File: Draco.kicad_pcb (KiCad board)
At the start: 2 copper layers, 114.3 x 44.5 mm, 117 parts, among them J1 Conn_01x03, J10 Conn_01x03, J11 Conn_01x06, J12 Conn_02x05_Odd_Even, J13 Conn_01x04, J14 Conn_01x01, J15 Micro_SD_Card, J16 Conn_01x03, J17 CHARGE_A, J18 CHARGE_C, J19 CHARGE_B, J2 Conn_01x03, J20 Conn_01x04, J3 Conn_01x03, J4 Conn_01x03, J5 Conn_01x03, J6 Conn_01x03, J7 Conn_01x03, J8 Conn_01x03, J9 Conn_01x03, Q1 BC817, Q2 Q_NMOS_DGS, Q3 BC817, Q4 Q_NMOS_DGS, Q5 BC817, Q6 Q_NMOS_DGS, U1 ATMEGA2560-16AU, U2 LOGIC-TXS0108EPWR(TSSOP20), U3 RFM95HW, U4 TPS54332, U5 TLV62568, U6 SAM-M8Q, U7 BMX055, U8 MS5607, Y1 16MHz

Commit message: Routed 60%
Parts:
- removed J14: Conn_01x01, Pin_Headers:Pin_Header_Straight_1x01_Pitch2.54mm
- BT1, C25, C26, R2, R3, U2, U6: moved to F.Cu
- moved U7 257.4 mm to (140.5, 82.6), turned to 90 degrees
- moved AE1 190.1 mm to (166.4, 112.1), turned to 90 degrees
- moved U2 188.1 mm to (156.5, 98.5), turned to 90 degrees
- moved C14 185.9 mm to (166.4, 106.9), turned to 270 degrees
- moved U3 170.0 mm to (178.0, 105.1), turned to 180 degrees
- moved C28 168.9 mm to (224.3, 119.8), turned to 90 degrees
- moved R6 167.9 mm to (231.4, 118.8)
- moved C27 165.6 mm to (226.3, 119.8), turned to 90 degrees
- moved R27 164.4 mm to (236.0, 127.5)
- moved R28 163.4 mm to (235.9, 118.9)
- moved U8 157.2 mm to (232.7, 121.9)
- moved C8 143.3 mm to (243.6, 68.8)
- moved C1 143.3 mm to (245.7, 86.3)
- moved C6 143.3 mm to (244.9, 77.9)
- moved R1 143.3 mm to (240.5, 58.3)
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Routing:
- net /~FIRE_C: track 1.92 -> 76.3 mm, vias 0 -> 2
- net /TEST_EN_C: track 0.00 -> 70.2 mm, vias 0 -> 4
- net /~FIRE_A: track 2.02 -> 71.4 mm, vias 0 -> 2
- net /~FIRE_B: track 1.90 -> 66.1 mm, vias 0 -> 2
- net /TEST_EN_A: track 0.00 -> 56.5 mm, vias 0 -> 2
- net /TEST_EN_B: track 0.00 -> 47.8 mm, vias 0 -> 2
- net /3V_SCK: track 6.27 -> 53.3 mm, vias 0 -> 3
- net /3V_MISO: track 6.87 -> 53.6 mm, vias 0 -> 1
- net /3V_MOSI: track 6.06 -> 52.7 mm, vias 0 -> 3
- net /TEST_READ_A: track 1.27 -> 38.9 mm, vias 0 -> 4
- net /TEST_READ_B: track 1.27 -> 33.3 mm, vias 0 -> 2
- net /CAM_LED: track 0.00 -> 26.5 mm
- net /3V_LORA_NSS: track 7.27 -> 32.6 mm, vias 0 -> 1
- net /5V_MISO: track 30.8 -> 55.5 mm, vias 2 -> 4
- net /3V_LORA_RST: track 9.28 -> 34.0 mm, vias 0 -> 1
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
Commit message: Routed 60%
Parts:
- renumbered REF** to MH1, REF** to MH2, REF** to MH3, REF** to MH4
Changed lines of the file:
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@@
     (tags "mounting hole 2.2mm m2")
     (attr virtual)
-    (fp_text reference REF** (at 0 -3.2) (layer F.SilkS)
+    (fp_text reference MH2 (at 0 -3.2) (layer F.SilkS)
       (effects (font (size 1 1) (thickness 0.15)))
     )
@@
     (tags "mounting hole 2.2mm m2")
     (attr virtual)
-    (fp_text reference REF** (at 0 -3.2) (layer F.SilkS)
+    (fp_text reference MH3 (at 0 -3.2) (layer F.SilkS)
       (effects (font (size 1 1) (thickness 0.15)))
     )
@@
     (tags "mounting hole 2.2mm m2")
     (attr virtual)
-    (fp_text reference REF** (at 0 -3.2) (layer F.SilkS)
+    (fp_text reference MH4 (at 0 -3.2) (layer F.SilkS)
       (effects (font (size 1 1) (thickness 0.15)))
     )
@@
     (tags "mounting hole 2.2mm m2")
     (attr virtual)
-    (fp_text reference REF** (at 0 -3.2) (layer F.SilkS)
+    (fp_text reference MH1 (at 0 -3.2) (layer F.SilkS)
       (effects (font (size 1 1) (thickness 0.15)))
     )
@@
   (segment (start 146.7396 94.012) (end 158.398 94.012) (width 0.25) (layer F.Cu) (net 62))
   (segment (start 158.398 94.012) (end 167.3352 85.0748) (width 0.25) (layer F.Cu) (net 62))
-  (segment (start 106.1847 92.3773) (end 106.1847 93.9927) (width 0.25) (layer F.Cu) (net 63) (status 400000))
-  (segment (start 151.353 90.012) (end 146.7396 90.012) (width 0.25) (layer F.Cu) (net 63) (status 800000))
+  (segment (start 106.1847 92.3773) (end 106.1847 93.9927) (width 0.25) (layer F.Cu) (net 63))
+  (segment (start 151.353 90.012) (end 146.7396 90.012) (width 0.25) (layer F.Cu) (net 63))
   (segment (start 152.3492 91.0082) (end 151.353 90.012) (width 0.25) (layer F.Cu) (net 63))
   (segment (start 152.3492 92.5322) (end 152.3492 91.0082) (width 0.25) (layer F.Cu) (net 63))
@@
   (segment (start 106.807 94.615) (end 109.347 94.615) (width 0.25) (layer F.Cu) (net 63))
   (segment (start 106.1847 93.9927) (end 106.807 94.615) (width 0.25) (layer F.Cu) (net 63))
-  (segment (start 104.2797 93.6523) (end 105.9028 95.2754) (width 0.25) (layer F.Cu) (net 64) (status 400000))
-  (segment (start 134.5396 91.4188) (end 134.5396 88.312) (width 0.25) (layer F.Cu) (net 64) (status 800000))
+  (segment (start 104.2797 93.6523) (end 105.9028 95.2754) (width 0.25) (layer F.Cu) (net 64))
+  (segment (start 134.5396 91.4188) (end 134.5396 88.312) (width 0.25) (layer F.Cu) (net 64))
   (segment (start 134.2136 91.7448) (end 134.5396 91.4188) (width 0.25) (layer F.Cu) (net 64))
   (segment (start 134.2136 94.5388) (end 134.2136 91.7448) (width 0.25) (layer F.Cu) (net 64))
@@
   (segment (start 105.9028 95.2754) (end 106.6292 95.2754) (width 0.25) (layer F.Cu) (net 64))
   (segment (start 104.2797 93.6523) (end 104.2797 92.3773) (width 0.25) (layer F.Cu) (net 64))
-  (segment (start 84.8614 99.7306) (end 84.8614 100.2538) (width 0.25) (layer F.Cu) (net 65) (status 400000))
-  (segment (start 144.0396 93.8822) (end 144.0396 88.312) (width 0.25) (layer F.Cu) (net 65) (status 800000))
+  (segment (start 84.8614 99.7306) (end 84.8614 100.2538) (width 0.25) (layer F.Cu) (net 65))
+  (segment (start 144.0396 93.8822) (end 144.0396 88.312) (width 0.25) (layer F.Cu) (net 65))
   (segment (start 143.129 94.7928) (end 144.0396 93.8822) (width 0.25) (layer F.Cu) (net 65))
   (segment (start 138.5316 94.7928) (end 143.129 94.7928) (width 0.25) (layer F.Cu) (net 65))
@@
   (segment (start 82.9818 99.7306) (end 84.8614 99.7306) (width 0.25) (layer F.Cu) (net 65))
   (segment (start 82.9818 99.7306) (end 82.9818 99.7102) (width 0.25) (layer F.Cu) (net 65))
-  (segment (start 102.3747 92.3773) (end 102.3747 93.0275) (width 0.25) (layer F.Cu) (net 66) (status 400000))
-  (segment (start 150.1178 91.012) (end 146.7396 91.012) (width 0.25) (layer F.Cu) (net 66) (status 800000))
+  (segment (start 102.3747 92.3773) (end 102.3747 93.0275) (width 0.25) (layer F.Cu) (net 66))
+  (segment (start 150.1178 91.012) (end 146.7396 91.012) (width 0.25) (layer F.Cu) (net 66))
   (segment (start 150.495 91.3892) (end 150.1178 91.012) (width 0.25) (layer F.Cu) (net 66))
   (via (at 150.495 91.3892) (size 0.6) (drill 0.4) (layers F.Cu B.Cu) (net 66))
@@
   (segment (start 102.3747 93.0275) (end 102.87 93.5228) (width 0.25) (layer F.Cu) (net 66))
   (segment (start 100.4697 93.6523) (end 100.4697 92.3773) (width 0.25) (layer F.Cu) (net 67))
-  (segment (start 109.9947 92.3773) (end 110.0734 92.456) (width 0.25) (layer F.Cu) (net 68) (status C00000))
-  (segment (start 110.0734 92.456) (end 118.7958 92.456) (width 0.25) (layer F.Cu) (net 68) (status 400000))
+  (segment (start 109.9947 92.3773) (end 110.0734 92.456) (width 0.25) (layer F.Cu) (net 68))
+  (segment (start 110.0734 92.456) (end 118.7958 92.456) (width 0.25) (layer F.Cu) (net 68))
   (via (at 118.7958 92.456) (size 0.6) (drill 0.4) (layers F.Cu B.Cu) (net 68))
   (segment (start 118.7958 92.456) (end 151.3078 92.456) (width 0.25) (layer B.Cu) (net 68))
@@
   (segment (start 151.3332 92.4814) (end 151.3332 90.678) (width 0.25) (layer F.Cu) (net 68))
   (segment (start 151.3332 90.678) (end 151.1672 90.512) (width 0.25) (layer F.Cu) (net 68))
-  (segment (start 151.1672 90.512) (end 146.7396 90.512) (width 0.25) (layer F.Cu) (net 68) (status 800000))
-  (segment (start 81.0514 99.7306) (end 81.0514 100.1014) (width 0.25) (layer F.Cu) (net 69) (status 400000))
-  (segment (start 145.2118 88.4842) (end 145.0396 88.312) (width 0.25) (layer F.Cu) (net 69) (status 800000))
+  (segment (start 151.1672 90.512) (end 146.7396 90.512) (width 0.25) (layer F.Cu) (net 68))
+  (segment (start 81.0514 99.7306) (end 81.0514 100.1014) (width 0.25) (layer F.Cu) (net 69))
+  (segment (start 145.2118 88.4842) (end 145.0396 88.312) (width 0.25) (layer F.Cu) (net 69))
   (segment (start 145.2118 94.4372) (end 145.2118 88.4842) (width 0.25) (layer F.Cu) (net 69))
   (segment (start 142.5194 97.1296) (end 145.2118 94.4372) (width 0.25) (layer F.Cu) (net 69))
@@
   (segment (start 81.0514 99.7306) (end 81.0514 99.7458) (width 0.25) (layer F.Cu) (net 69))
   (segment (start 79.1718 99.7306) (end 79.1718 99.7102) (width 0.25) (layer F.Cu) (net 69))
-  (segment (start 108.0897 93.6523) (end 117.5741 93.6523) (width 0.25) (layer F.Cu) (net 70) (status 400000))
-  (segment (start 135.0396 93.1296) (end 135.0396 88.312) (width 0.25) (layer F.Cu) (net 70) (status 800000))
+  (segment (start 108.0897 93.6523) (end 117.5741 93.6523) (width 0.25) (layer F.Cu) (net 70))
+  (segment (start 135.0396 93.1296) (end 135.0396 88.312) (width 0.25) (layer F.Cu) (net 70))
   (segment (start 135.0518 93.1418) (end 135.0396 93.1296) (width 0.25) (layer F.Cu) (net 70))
   (via (at 135.0518 93.1418) (size 0.6) (drill 0.4) (layers F.Cu B.Cu) (net 70))
@@
   (segment (start 117.5741 93.6523) (end 118.0846 93.1418) (width 0.25) (layer F.Cu) (net 70))
   (segment (start 108.0897 93.6523) (end 108.0897 92.3773) (width 0.25) (layer F.Cu) (net 70))
-  (segment (start 144.5396 88.312) (end 144.5396 94.2966) (width 0.25) (layer F.Cu) (net 71) (status 400000))
+  (segment (start 144.5396 88.312) (end 144.5396 94.2966) (width 0.25) (layer F.Cu) (net 71))
   (segment (start 143.256 95.5802) (end 144.5396 94.2966) (width 0.25) (layer F.Cu) (net 71))
-  (segment (start 91.0336 97.6884) (end 88.9914 99.7306) (width 0.25) (layer F.Cu) (net 71) (status 800000))
+  (segment (start 91.0336 97.6884) (end 88.9914 99.7306) (width 0.25) (layer F.Cu) (net 71))
   (via (at 139.2174 95.5802) (size 0.6) (drill 0.4) (layers F.Cu B.Cu) (net 71))
   (segment (start 118.8212 95.5802) (end 139.2174 95.5802) (width 0.25) (layer B.Cu) (net 71))
@@
   (segment (start 91.0336 97.6884) (end 101.7524 97.6884) (width 0.25) (layer F.Cu) (net 71))
   (segment (start 139.2174 95.5802) (end 143.256 95.5802) (width 0.25) (layer F.Cu) (net 71))
-  (segment (start 88.6206 99.7306) (end 88.9914 99.7306) (width 0.25) (layer F.Cu) (net 71) (status C00000))
+  (segment (start 88.6206 99.7306) (end 88.9914 99.7306) (width 0.25) (layer F.Cu) (net 71))
   (segment (start 86.741 99.7306) (end 88.6206 99.7306) (width 0.25) (layer F.Cu) (net 71))
   (segment (start 86.741 99.7306) (end 86.741 99.7102) (width 0.25) (layer F.Cu) (net 71))

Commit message: Backtracked to 30%
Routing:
- net /~FIRE_C: track 76.3 -> 2.11 mm, vias 2 -> 0
- net /TEST_EN_C: track 70.2 -> 0.00 mm, vias 4 -> 0
- net /~FIRE_A: track 71.4 -> 2.36 mm, vias 2 -> 0
- net /~FIRE_B: track 66.1 -> 2.27 mm, vias 2 -> 0
- net /TEST_EN_A: track 56.5 -> 0.00 mm, vias 2 -> 0
- net /5V_MISO: track 55.5 -> 0.36 mm, vias 4 -> 0
- net /3V_MISO: track 53.6 -> 0.59 mm, vias 1 -> 0
- net /3V_SCK: track 53.3 -> 0.91 mm, vias 3 -> 0
- net /3V_MOSI: track 52.7 -> 0.51 mm, vias 3 -> 0
- net /5V_SCK: track 51.7 -> 0.20 mm, vias 2 -> 0
- net /TEST_EN_B: track 47.8 -> 0.11 mm, vias 2 -> 0
- net /5V_MOSI: track 46.0 -> 0.00 mm, vias 2 -> 0
- net /RESET: track 45.8 -> 1.57 mm, vias 3 -> 0
- net /TEST_READ_A: track 38.9 -> 1.27 mm, vias 4 -> 0
- net GND: track 338.7 -> 302.4 mm, vias 9 -> 3
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
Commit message: Finished left side
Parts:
- moved C9 167.0 mm to (119.5, 101.9)
- moved C11 163.1 mm to (113.0, 88.7), turned to 180 degrees
- moved R1 110.8 mm to (132.4, 82.8), turned to 180 degrees
- moved C12 74.1 mm to (237.7, 97.4)
- moved C2 63.0 mm to (234.9, 135.2)
- moved L1 59.0 mm to (226.7, 97.0)
- moved C8 46.5 mm to (223.8, 110.8)
- moved C1 42.5 mm to (247.6, 128.7)
- moved C10 42.5 mm to (245.8, 116.5)
- moved C6 42.5 mm to (246.8, 120.3)
- moved C3 42.5 mm to (247.3, 133.5)
- moved C25 27.9 mm to (220.4, 107.6)
- moved U8 12.7 mm to (234.9, 109.5), turned to 90 degrees
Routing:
- net /VBAT2: track 1.88 -> 79.0 mm, vias 0 -> 4
- net /~FIRE_C: track 2.11 -> 76.1 mm, vias 0 -> 2
- net /~FIRE_A: track 2.36 -> 69.0 mm, vias 0 -> 2
- net /~FIRE_B: track 2.27 -> 67.0 mm, vias 0 -> 4
- net /TEST_EN_C: track 0.00 -> 57.4 mm, vias 0 -> 4
- net /VBAT: track 0.00 -> 53.8 mm, vias 0 -> 2
- net /TEST_EN_A: track 0.00 -> 50.1 mm, vias 0 -> 4
- net /TEST_EN_B: track 0.11 -> 49.7 mm, vias 0 -> 4
- net /TEST_READ_C: track 1.27 -> 41.6 mm, vias 0 -> 4
- net /TEST_READ_A: track 1.27 -> 36.1 mm, vias 0 -> 4
- net Net-(J19-Pad2): track 12.3 -> 46.7 mm, vias 0 -> 1
- net +5V: track 42.5 -> 76.4 mm, vias 2 -> 3
- net Net-(BT1-Pad1): track 34.1 -> 1.50 mm
- net /TEST_READ_B: track 1.27 -> 32.2 mm, vias 0 -> 4
- net GND: track 302.4 -> 331.1 mm, vias 3 -> 7
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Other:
- rule trace_min: 0.2 -> 0.1524

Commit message: 80% done routing
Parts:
- added J14: Conn_01x01, Pin_Headers:Pin_Header_Straight_1x01_Pitch2.54mm, F.Cu at (169.0, 116.8)
- moved C1 178.1 mm to (70.4, 146.8)
- moved C6 178.0 mm to (70.0, 140.9)
- moved C3 177.2 mm to (70.4, 144.2)
- moved C10 177.0 mm to (70.1, 137.9)
- moved C26 168.8 mm to (64.5, 135.3), turned to 90 degrees
- moved C28 165.8 mm to (59.3, 135.6)
- moved C25 165.7 mm to (57.1, 135.8)
- moved C2 165.4 mm to (70.2, 150.9)
- moved C27 165.4 mm to (61.6, 135.5)
- moved C8 155.8 mm to (70.0, 135.6)
- moved R6 135.8 mm to (96.1, 106.7), turned to 180 degrees
- moved C12 106.2 mm to (132.1, 86.4), turned to 180 degrees
- moved L1 97.8 mm to (129.3, 88.0), turned to 90 degrees
- moved C29 72.8 mm to (181.2, 84.2), turned to 270 degrees
- moved R27 68.2 mm to (183.5, 84.0), turned to 270 degrees
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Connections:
- L1 pad 1: Net-(L1-Pad1) -> +5V
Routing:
- net +3V3: track 20.5 -> 178.8 mm, vias 0 -> 5
- net GND: track 331.1 -> 464.9 mm, vias 7 -> 17
- net +5V: track 76.4 -> 187.1 mm, vias 3 -> 5
- net /3V_SDA: track 0.10 -> 57.8 mm, vias 0 -> 4
- net /GPS_TXD: track 0.00 -> 53.7 mm, vias 0 -> 4
- net /3V_MISO: track 0.59 -> 52.7 mm, vias 0 -> 4
- net /3V_MOSI: track 0.51 -> 52.6 mm, vias 0 -> 1
- net /3V_SCK: track 0.91 -> 52.2 mm, vias 0 -> 3
- net Net-(R2-Pad2): track 0.00 -> 48.8 mm, vias 0 -> 2
- net /LORA_INT: track 0.00 -> 46.9 mm, vias 0 -> 1
- net Net-(BT1-Pad1): track 1.50 -> 36.0 mm
- net /SERVO10: track 0.00 -> 33.3 mm, vias 0 -> 2
- net /RESET: track 14.3 -> 46.4 mm, vias 1 -> 3
- net /3V_LORA_RST: track 1.64 -> 32.3 mm, vias 0 -> 1
- net /SERVO9: track 0.00 -> 30.4 mm, vias 0 -> 2
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
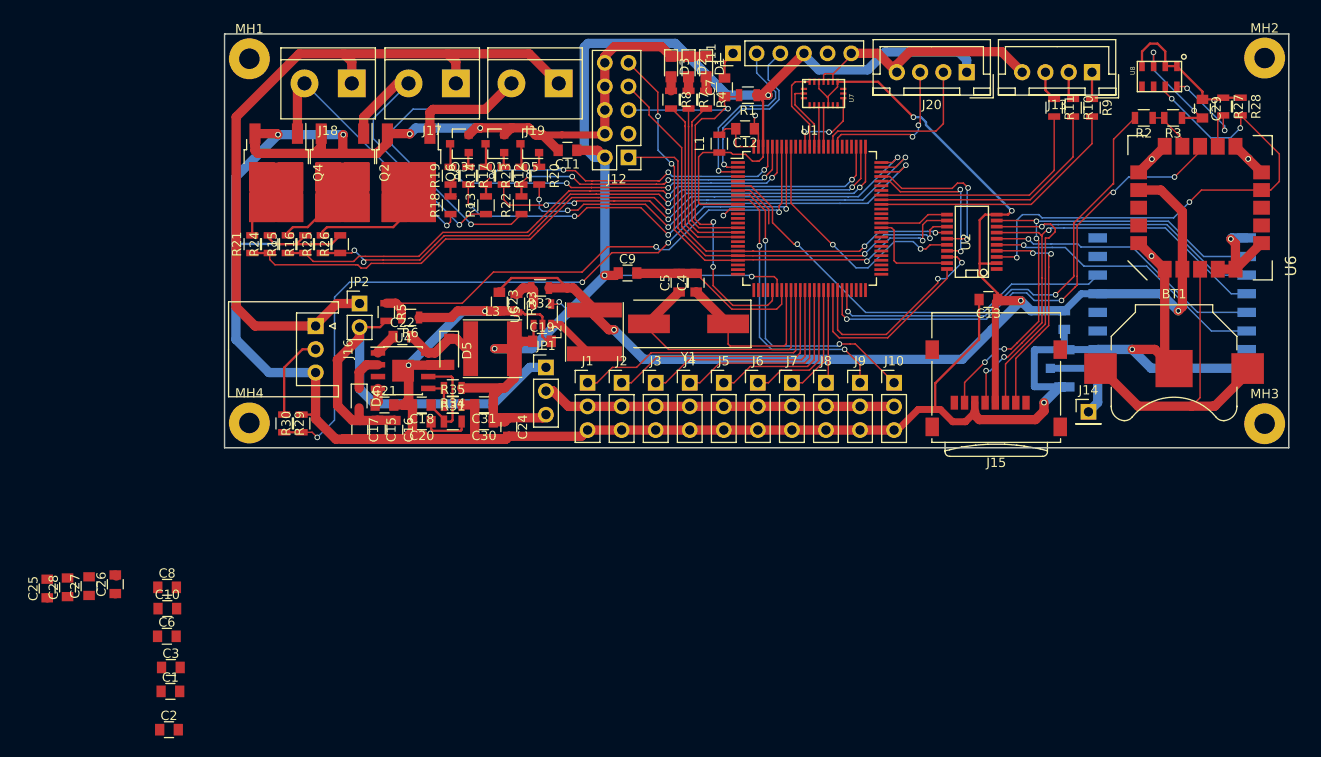
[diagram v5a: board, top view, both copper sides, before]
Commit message: Adding bypass capacitors
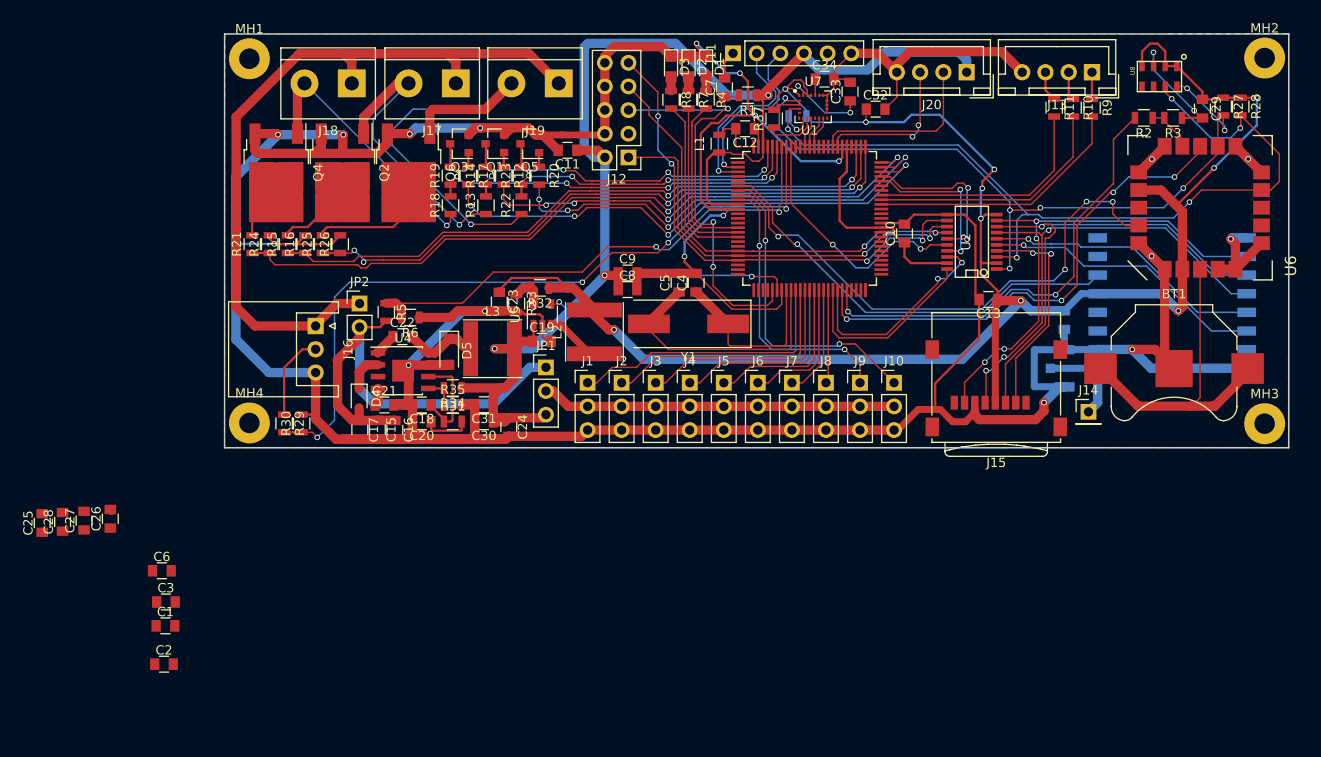
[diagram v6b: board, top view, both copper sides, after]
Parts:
- added C32: 100nF, Capacitors_SMD:C_0805, F.Cu at (146.1, 84.3)
- added C33: 100nF, Capacitors_SMD:C_0805, F.Cu at (143.4, 82.4)
- added C34: 10nF 16V, Capacitors_SMD:C_0805, F.Cu at (140.6, 81.1)
- added R36: 10k, Resistors_SMD:R_0805, B.Cu at (137.7, 85.0)
- added R37: 10k, Resistors_SMD:R_0805, F.Cu at (135.2, 85.3)
- U7: value BMX055 -> LSM9DS1TR‎; footprint Current_Control_Systems:BMX055 -> Housings_LGA:LGA-24L_3x3.5mm_Pitch0.43mm
- moved C10 88.8 mm to (149.2, 97.6), turned to 90 degrees
- moved C8 58.9 mm to (119.5, 103.7)
- moved C1 7.06 mm to (69.8, 139.8)
- moved C2 7.06 mm to (69.7, 143.9)
- moved C25 7.06 mm to (56.6, 128.7)
- moved C26 7.06 mm to (63.9, 128.3)
- moved C27 7.06 mm to (61.1, 128.5)
- moved C28 7.06 mm to (58.8, 128.6)
- moved C3 7.06 mm to (69.9, 137.2)
- moved C6 7.06 mm to (69.5, 133.9)
- moved U7 1.81 mm to (139.4, 84.0), turned to 0 degrees
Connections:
- U1 pad 85: /GYRO_INT1 -> Net-(U1-Pad85)
- U1 pad 86: /GYRO_INT2 -> Net-(U1-Pad86)
- U1 pad 87: /ACCEL_INT1 -> /ACCEL_INT2
- U1 pad 88: /ACCEL_INT2 -> /ACCEL_INT1
- U7 pad 1: /ACCEL_INT2 -> +3V3
- U7 pad 10: /MAGNET_INT1 -> Net-(U7-Pad10)
- U7 pad 11: /3V_SDA -> /ACCEL_INT1
- U7 pad 12: Net-(U7-Pad12) -> /ACCEL_INT2
- U7 pad 13: +3V3 -> Net-(U7-Pad13)
- U7 pad 14: /GYRO_INT1 -> GND
- U7 pad 15: /GYRO_INT2 -> GND
- U7 pad 16: Net-(U7-Pad16) -> GND
- U7 pad 17: Net-(U7-Pad17) -> GND
- U7 pad 18: (no net) -> GND
- U7 pad 19: /ACCEL_INT1 -> GND
- U7 pad 2: Net-(U7-Pad2) -> /3V_SCL
- U7 pad 20: Net-(U7-Pad20) -> GND
- U7 pad 4: GND -> /3V_SDA
- U7 pad 6: GND -> Net-(U7-Pad6)
- U7 pad 7: +3V3 -> Net-(R36-Pad1)
- U7 pad 8: (no net) -> Net-(R37-Pad1)
- U7 pad 9: /3V_SCL -> /MAGNET_INT1
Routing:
- net GND: track 464.9 -> 541.2 mm, vias 17 -> 21
- net /3V_SCL: track 13.1 -> 80.6 mm, vias 2 -> 7
- net /GPS_INT: track 5.71 -> 59.1 mm, vias 0 -> 4
- net /3V_SDA: track 57.8 -> 90.7 mm, vias 4 -> 5
- net +3V3: track 178.8 -> 210.5 mm, vias 5 -> 10
- net +5V: track 187.1 -> 198.9 mm
- net Net-(C33-Pad1): track 0.00 -> 9.31 mm, vias 0 -> 2
- net /ACCEL_INT2: track 9.48 -> 3.47 mm
- net Net-(R37-Pad1): track 0.00 -> 5.62 mm
- net /MAGNET_INT1: track 8.85 -> 3.34 mm, vias 2 -> 0
- net /GYRO_INT2: track 4.45 -> 0.00 mm
- net /GYRO_INT1: track 4.45 -> 0.00 mm
- net /ACCEL_INT1: track 7.51 -> 3.49 mm
- net Net-(R36-Pad1): track 0.00 -> 3.73 mm, vias 0 -> 1
- net Net-(C34-Pad1): track 0.00 -> 1.75 mm
- added copper zone on B.Cu, net GND
